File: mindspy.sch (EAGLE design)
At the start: 39 parts, among them IC1 ADS1298IPAG, IC2 TPS7A4901, X1 DF9-31S, X2 STELLARIS-LAUNCHPAD-HALF

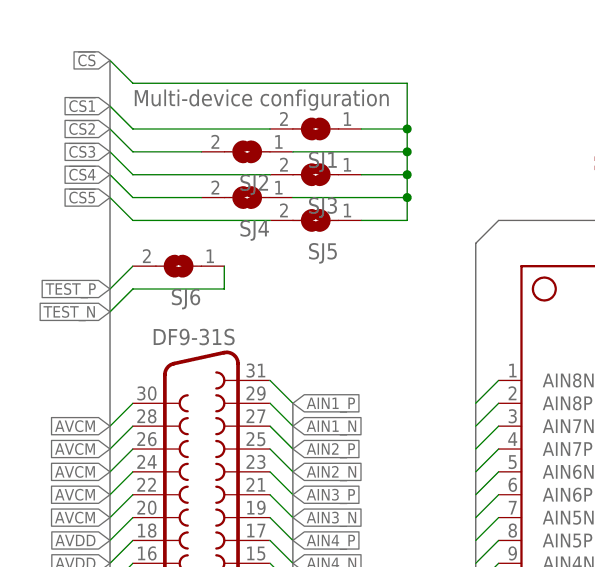
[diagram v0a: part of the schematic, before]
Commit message: add pads for RLD auxiliary input and rearrange wires
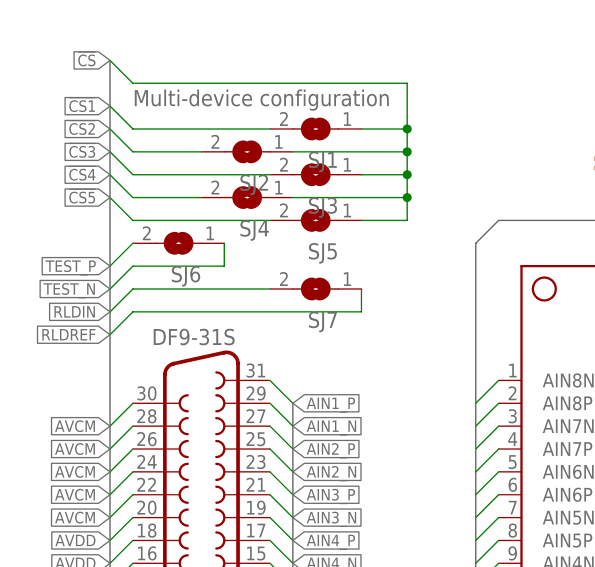
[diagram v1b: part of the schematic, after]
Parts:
- added SJ7: (no value), jumper:SJ
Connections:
- net RLDIN: now also SJ7.2
- net RLDREF: now also SJ7.1
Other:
- moved on the sheet: SJ6
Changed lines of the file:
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@@
 <part name="L5" library="fabhack" deviceset="L1210" device="" value="10u"/>
 <part name="SJ6" library="jumper" deviceset="SJ" device=""/>
+<part name="SJ7" library="jumper" deviceset="SJ" device=""/>
 </parts>
 <sheets>
@@
 <instance part="L4" gate="G$1" x="154.94" y="116.84" rot="R90"/>
 <instance part="L5" gate="G$1" x="154.94" y="109.22" rot="R90"/>
-<instance part="SJ6" gate="1" x="20.32" y="104.14" rot="R180"/>
+<instance part="SJ6" gate="1" x="20.32" y="106.68" rot="R180"/>
+<instance part="SJ7" gate="1" x="35.56" y="101.6" rot="R180"/>
 </instances>
 <busses>
@@
 <wire x1="78.74" y1="109.22" x2="81.28" y2="106.68" width="0.1524" layer="91"/>
 </segment>
+<segment>
+<wire x1="12.7" y1="96.52" x2="15.24" y2="99.06" width="0.1524" layer="91"/>
+<label x="12.7" y="96.52" size="1.27" layer="95" rot="R180" xref="yes"/>
+<pinref part="SJ7" gate="1" pin="1"/>
+<wire x1="40.64" y1="101.6" x2="40.64" y2="99.06" width="0.1524" layer="91"/>
+<wire x1="40.64" y1="99.06" x2="15.24" y2="99.06" width="0.1524" layer="91"/>
+</segment>
 </net>
 <net name="RLDOUT" class="0">
@@
 <wire x1="73.66" y1="109.22" x2="76.2" y2="106.68" width="0.1524" layer="91"/>
 </segment>
+<segment>
+<wire x1="12.7" y1="99.06" x2="15.24" y2="101.6" width="0.1524" layer="91"/>
+<label x="12.7" y="99.06" size="1.27" layer="95" rot="R180" xref="yes"/>
+<pinref part="SJ7" gate="1" pin="2"/>
+<wire x1="15.24" y1="101.6" x2="30.48" y2="101.6" width="0.1524" layer="91"/>
+</segment>
 </net>
 <net name="RLDINV" class="0">
@@
 </segment>
 <segment>
+<wire x1="12.7" y1="104.14" x2="15.24" y2="106.68" width="0.1524" layer="91"/>
+<label x="12.7" y="104.14" size="1.27" layer="95" rot="R180" xref="yes"/>
+<pinref part="SJ6" gate="1" pin="2"/>
+</segment>
+</net>
+<net name="TEST_N" class="0">
+<segment>
+<pinref part="IC1" gate="G$1" pin="TESTN_PACE_OUT2"/>
+<wire x1="71.12" y1="35.56" x2="73.66" y2="38.1" width="0.1524" layer="91"/>
+</segment>
+<segment>
 <wire x1="12.7" y1="101.6" x2="15.24" y2="104.14" width="0.1524" layer="91"/>
 <label x="12.7" y="101.6" size="1.27" layer="95" rot="R180" xref="yes"/>
-<pinref part="SJ6" gate="1" pin="2"/>
-</segment>
-</net>
-<net name="TEST_N" class="0">
-<segment>
-<pinref part="IC1" gate="G$1" pin="TESTN_PACE_OUT2"/>
-<wire x1="71.12" y1="35.56" x2="73.66" y2="38.1" width="0.1524" layer="91"/>
-</segment>
-<segment>
-<wire x1="12.7" y1="99.06" x2="15.24" y2="101.6" width="0.1524" layer="91"/>
-<label x="12.7" y="99.06" size="1.27" layer="95" rot="R180" xref="yes"/>
 <pinref part="SJ6" gate="1" pin="1"/>
-<wire x1="15.24" y1="101.6" x2="25.4" y2="101.6" width="0.1524" layer="91"/>
-<wire x1="25.4" y1="101.6" x2="25.4" y2="104.14" width="0.1524" layer="91"/>
-</segment>
-</net>
+<wire x1="15.24" y1="104.14" x2="25.4" y2="104.14" width="0.1524" layer="91"/>
+<wire x1="25.4" y1="104.14" x2="25.4" y2="106.68" width="0.1524" layer="91"/>
+</segment>
+</net>

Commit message: finalization, fixes in layers
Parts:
- IC2: device fabhack:TPS7A4901 -> ti:TPS7A4901
- X1: device con-hirose:DF9-31S -> hirose:DF9-31S
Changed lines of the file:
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@@
 <part name="C23" library="rcl" deviceset="C-EU" device="C0402" value="1u"/>
 <part name="C10" library="rcl" deviceset="C-EU" device="C0402" value="1u"/>
-<part name="X1" library="con-hirose" deviceset="DF9-31S" device=""/>
+<part name="X1" library="hirose" deviceset="DF9-31S" device=""/>
 <part name="+3V1" library="supply1" deviceset="+3V3" device=""/>
 <part name="GND1" library="supply1" deviceset="GND" device=""/>
@@
 <part name="P+2" library="supply1" deviceset="+5V" device=""/>
 <part name="SJ13" library="jumper" deviceset="SJ" device=""/>
-<part name="IC2" library="fabhack" deviceset="TPS7A49*" device="" technology="01"/>
+<part name="IC2" library="ti" deviceset="TPS7A49*" device="" technology="01"/>
 <part name="R1" library="rcl" deviceset="R-EU_" device="R0402"/>
 <part name="R2" library="rcl" deviceset="R-EU_" device="R0402"/>

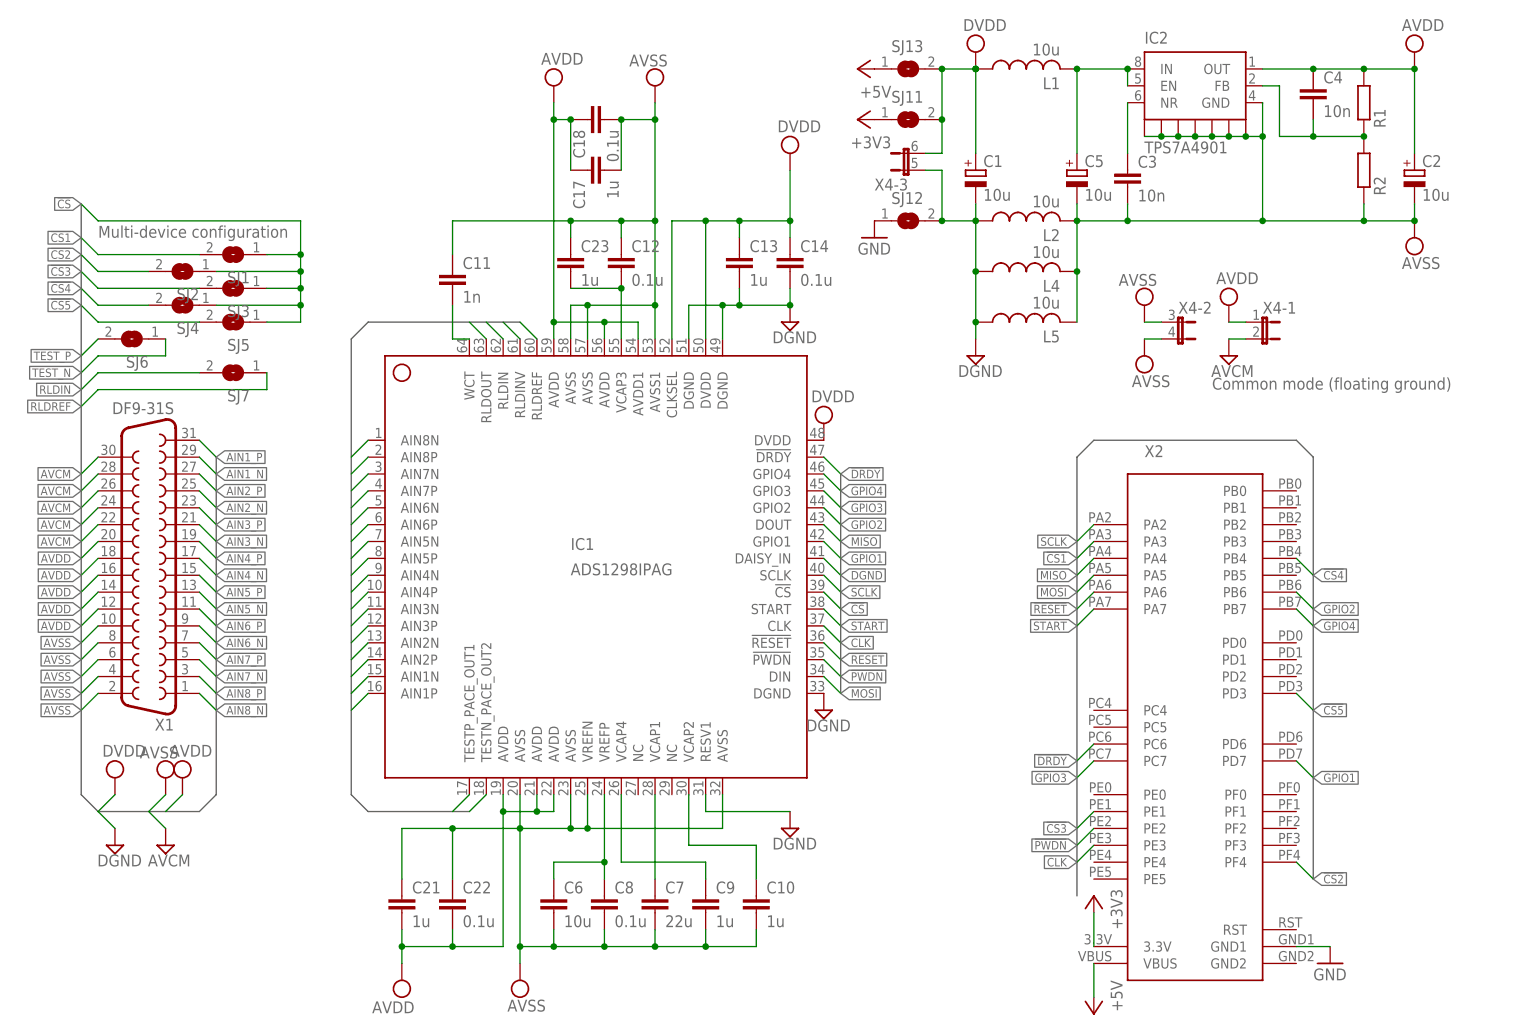
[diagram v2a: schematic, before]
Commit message: fix part values
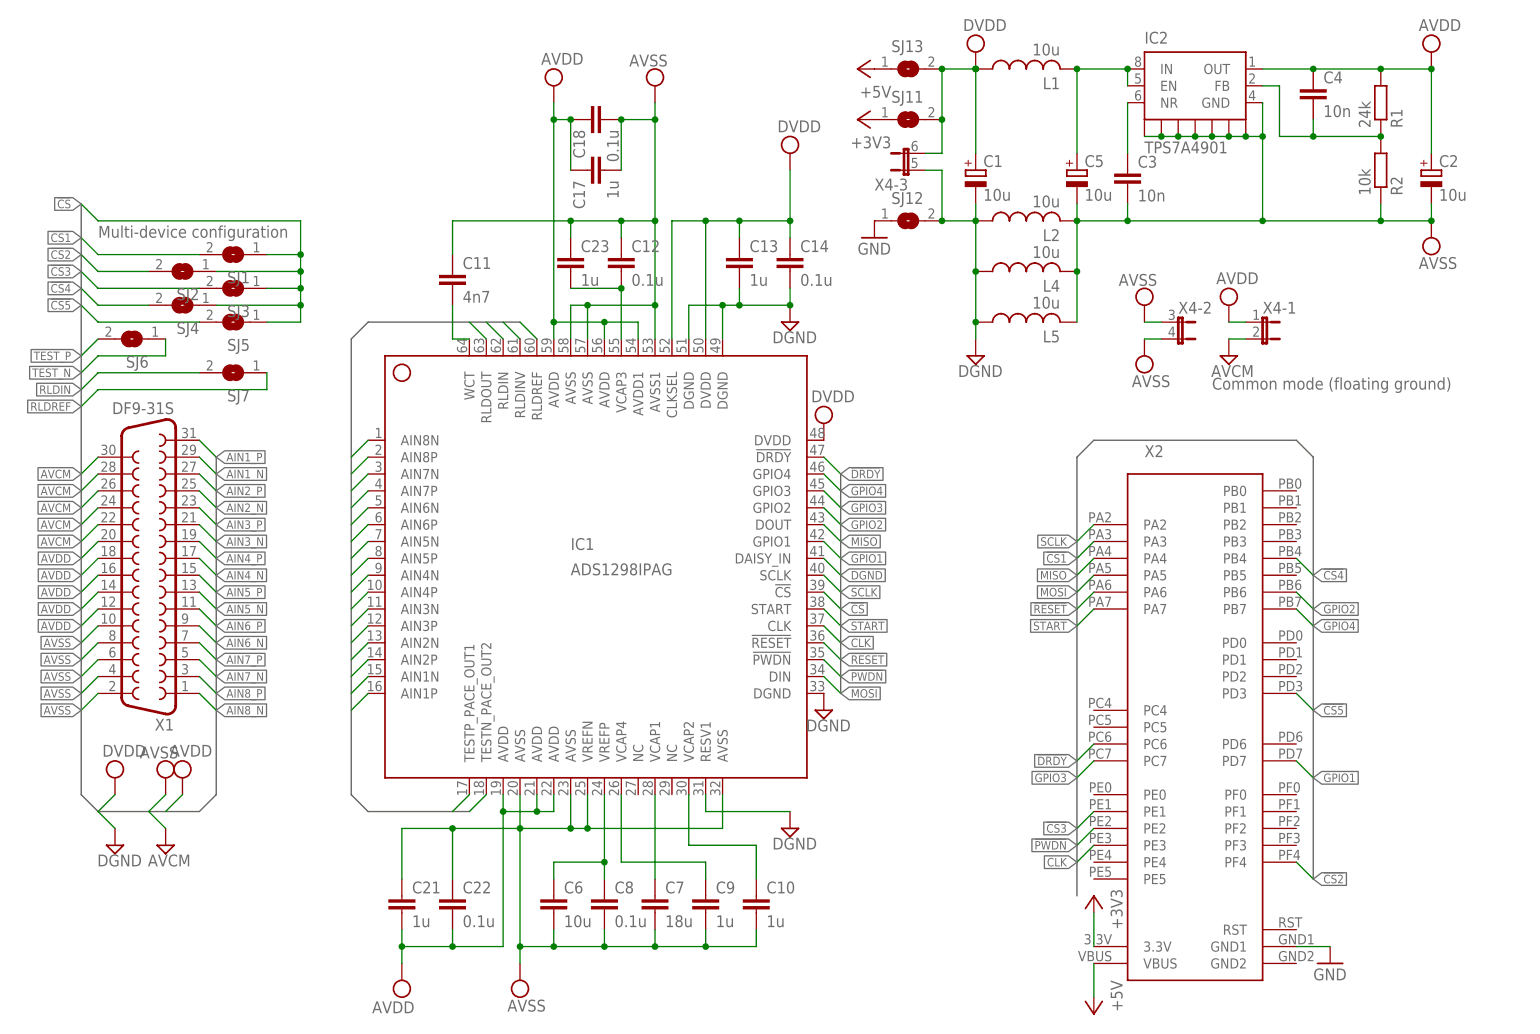
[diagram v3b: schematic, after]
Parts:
- C11: value 1n -> 4n7
- C7: value 22u -> 18u
- R1: value (none) -> 24k
- R2: value (none) -> 10k
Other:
- moved on the sheet: C2, R1, R2
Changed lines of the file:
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@@
 <part name="SUPPLY19" library="supply2" deviceset="VSS" device="" value="AVSS"/>
 <part name="C6" library="rcl" deviceset="C-EU" device="C0805" value="10u"/>
-<part name="C7" library="rcl" deviceset="C-EU" device="C0805" value="22u"/>
+<part name="C7" library="rcl" deviceset="C-EU" device="C0805" value="18u"/>
 <part name="C8" library="rcl" deviceset="C-EU" device="C0402" value="0.1u"/>
 <part name="C9" library="rcl" deviceset="C-EU" device="C0402" value="1u"/>
 <part name="SUPPLY21" library="supply2" deviceset="DGND" device=""/>
-<part name="C11" library="rcl" deviceset="C-EU" device="C0402" value="1n"/>
+<part name="C11" library="rcl" deviceset="C-EU" device="C0402" value="4n7"/>
 <part name="C12" library="rcl" deviceset="C-EU" device="C0402" value="0.1u"/>
 <part name="C13" library="rcl" deviceset="C-EU" device="C0402" value="1u"/>
@@
 <part name="SJ13" library="jumper" deviceset="SJ" device=""/>
 <part name="IC2" library="ti" deviceset="TPS7A49*" device="" technology="01"/>
-<part name="R1" library="rcl" deviceset="R-EU_" device="R0402"/>
-<part name="R2" library="rcl" deviceset="R-EU_" device="R0402"/>
+<part name="R1" library="rcl" deviceset="R-EU_" device="R0402" value="24k"/>
+<part name="R2" library="rcl" deviceset="R-EU_" device="R0402" value="10k"/>
 <part name="C2" library="rcl" deviceset="CPOL-EU" device="SMCA" value="10u"/>
 <part name="X4" library="jumper" deviceset="JP3QE" device=""/>
@@
 <instance part="SUPPLY7" gate="G$1" x="147.32" y="104.14"/>
 <instance part="SUPPLY10" gate="G$1" x="147.32" y="149.86"/>
-<instance part="SUPPLY8" gate="G$1" x="213.36" y="121.92"/>
-<instance part="SUPPLY9" gate="G$1" x="213.36" y="149.86"/>
+<instance part="SUPPLY8" gate="G$1" x="215.9" y="121.92"/>
+<instance part="SUPPLY9" gate="G$1" x="215.9" y="149.86"/>
 <instance part="L1" gate="G$1" x="154.94" y="147.32" rot="R90"/>
 <instance part="L2" gate="G$1" x="154.94" y="124.46" rot="R90"/>
@@
 <instance part="IC2" gate="G$1" x="180.34" y="144.78"/>
 <instance part="IC2" gate="G$2" x="180.34" y="137.16"/>
-<instance part="R1" gate="G$1" x="205.74" y="142.24" rot="MR90"/>
-<instance part="R2" gate="G$1" x="205.74" y="132.08" rot="MR90"/>
-<instance part="C2" gate="G$1" x="213.36" y="132.08"/>
+<instance part="R1" gate="G$1" x="208.28" y="142.24" rot="MR90"/>
+<instance part="R2" gate="G$1" x="208.28" y="132.08" rot="MR90"/>
+<instance part="C2" gate="G$1" x="215.9" y="132.08"/>
 <instance part="X4" gate="-1" x="190.5" y="109.22" rot="R270"/>
 <instance part="X4" gate="-2" x="177.8" y="109.22" rot="R270"/>
@@
 <junction x="190.5" y="124.46"/>
 <pinref part="SUPPLY8" gate="G$1" pin="VSS"/>
-<wire x1="190.5" y1="124.46" x2="205.74" y2="124.46" width="0.1524" layer="91"/>
-<junction x="213.36" y="124.46"/>
+<wire x1="190.5" y1="124.46" x2="208.28" y2="124.46" width="0.1524" layer="91"/>
+<junction x="215.9" y="124.46"/>
 <pinref part="C2" gate="G$1" pin="-"/>
-<wire x1="205.74" y1="124.46" x2="213.36" y2="124.46" width="0.1524" layer="91"/>
-<wire x1="213.36" y1="124.46" x2="213.36" y2="127" width="0.1524" layer="91"/>
+<wire x1="208.28" y1="124.46" x2="215.9" y2="124.46" width="0.1524" layer="91"/>
+<wire x1="215.9" y1="124.46" x2="215.9" y2="127" width="0.1524" layer="91"/>
 <pinref part="R2" gate="G$1" pin="1"/>
-<wire x1="205.74" y1="127" x2="205.74" y2="124.46" width="0.1524" layer="91"/>
-<junction x="205.74" y="124.46"/>
+<wire x1="208.28" y1="127" x2="208.28" y2="124.46" width="0.1524" layer="91"/>
+<junction x="208.28" y="124.46"/>
 <pinref part="L4" gate="G$1" pin="2"/>
 <wire x1="162.56" y1="109.22" x2="162.56" y2="116.84" width="0.1524" layer="91"/>
@@
 <pinref part="SUPPLY9" gate="G$1" pin="VCC"/>
 <pinref part="C2" gate="G$1" pin="+"/>
-<wire x1="213.36" y1="134.62" x2="213.36" y2="147.32" width="0.1524" layer="91"/>
+<wire x1="215.9" y1="134.62" x2="215.9" y2="147.32" width="0.1524" layer="91"/>
 <pinref part="R1" gate="G$1" pin="2"/>
-<wire x1="205.74" y1="147.32" x2="213.36" y2="147.32" width="0.1524" layer="91"/>
-<junction x="213.36" y="147.32"/>
+<wire x1="208.28" y1="147.32" x2="215.9" y2="147.32" width="0.1524" layer="91"/>
+<junction x="215.9" y="147.32"/>
 <pinref part="IC2" gate="G$1" pin="OUT"/>
 <pinref part="C4" gate="G$1" pin="1"/>
 <wire x1="190.5" y1="147.32" x2="198.12" y2="147.32" width="0.1524" layer="91"/>
-<wire x1="198.12" y1="147.32" x2="205.74" y2="147.32" width="0.1524" layer="91"/>
+<wire x1="198.12" y1="147.32" x2="208.28" y2="147.32" width="0.1524" layer="91"/>
 <junction x="198.12" y="147.32"/>
-<junction x="205.74" y="147.32"/>
+<junction x="208.28" y="147.32"/>
 </segment>
 <segment>
@@
 <pinref part="R1" gate="G$1" pin="1"/>
 <pinref part="R2" gate="G$1" pin="2"/>
-<wire x1="205.74" y1="137.16" x2="198.12" y2="137.16" width="0.1524" layer="91"/>
+<wire x1="208.28" y1="137.16" x2="198.12" y2="137.16" width="0.1524" layer="91"/>
 <wire x1="198.12" y1="137.16" x2="193.04" y2="137.16" width="0.1524" layer="91"/>
 <wire x1="193.04" y1="137.16" x2="193.04" y2="144.78" width="0.1524" layer="91"/>
 <pinref part="IC2" gate="G$1" pin="FB"/>
 <wire x1="193.04" y1="144.78" x2="190.5" y2="144.78" width="0.1524" layer="91"/>
-<junction x="205.74" y="137.16"/>
+<junction x="208.28" y="137.16"/>
 <pinref part="C4" gate="G$1" pin="2"/>
 <wire x1="198.12" y1="139.7" x2="198.12" y2="137.16" width="0.1524" layer="91"/>
